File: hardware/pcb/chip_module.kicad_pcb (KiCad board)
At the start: 6 copper layers, 150 x 140 mm, 201 parts, among them J12 BTB_DAUGHTER

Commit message: latest boards 2 pcb first route
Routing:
- net +5V_A: track 8.44 -> 328.6 mm, vias 0 -> 17
- net DET_REF: track 1.00 -> 303.8 mm, vias 1 -> 3
- net DET_IN56: track 1.00 -> 261.4 mm, vias 1 -> 7
- net DET_IN61: track 1.00 -> 252.0 mm, vias 1 -> 6
- net DET_IN25: track 1.00 -> 239.3 mm, vias 1 -> 10
- net DET_IN30: track 1.00 -> 237.6 mm, vias 1 -> 6
- net DET_IN31: track 1.00 -> 235.3 mm, vias 1 -> 5
- net DET_IN16: track 1.00 -> 234.6 mm, vias 1 -> 10
- net DET_IN48: track 1.00 -> 230.7 mm, vias 1 -> 9
- net DET_IN20: track 1.00 -> 227.8 mm, vias 1 -> 5
- net DET_IN55: track 1.00 -> 227.3 mm, vias 1 -> 8
- net DET_IN23: track 1.00 -> 222.7 mm, vias 1 -> 8
- net DET_IN19: track 1.00 -> 221.4 mm, vias 1 -> 5
- net DET_IN17: track 1.00 -> 221.3 mm, vias 1 -> 9
- net DET_IN8: track 1.00 -> 203.2 mm, vias 1 -> 5
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
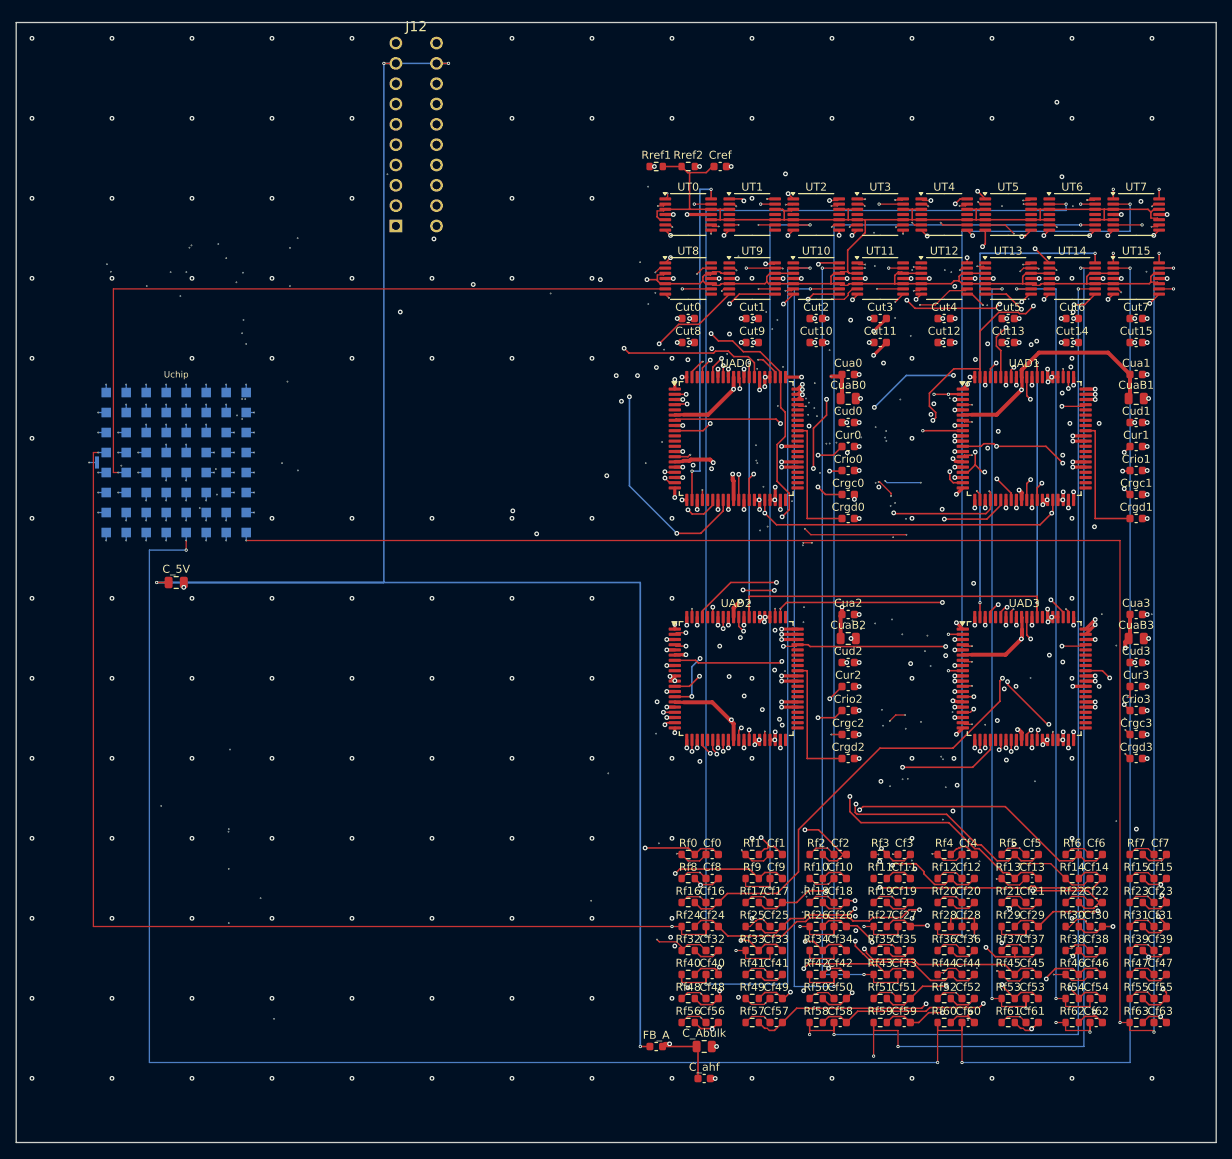
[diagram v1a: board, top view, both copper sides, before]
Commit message: pcb: head board DRC-clean for production (749 -> 0 violations)
- Remove 935 FreeRouting signal tracks incorrectly placed on In1.Cu (GND plane)
- Remove 41 sub-min-width FreeRouting stubs (0.1124mm < 0.15mm min) on F.Cu DET_IN*
- Remove redundant DET_IN30 through-via at (34.246,28.153): net stays fully
  connected via its In3 route + via at (132.083,22.955); clears 3 In3 clearance
  conflicts in the packed x~34 channel (DET_IN8/DET_IN19/DET_IN30)
- Remove zero-length FreeRouting stubs (<0.05mm)
- Relax hole-to-hole min 0.2495mm -> 0.22mm: HDI-appropriate for 0.10mm laser
  drills (JLCPCB/PCBWay HDI support 0.15mm); clears 3 hole_near_hole pairs
- Re-fill both copper zones (GND/In1, +3V3/In2) to clear stale-pour violations

Final: kicad-cli DRC 0 violations / 0 unconnected.
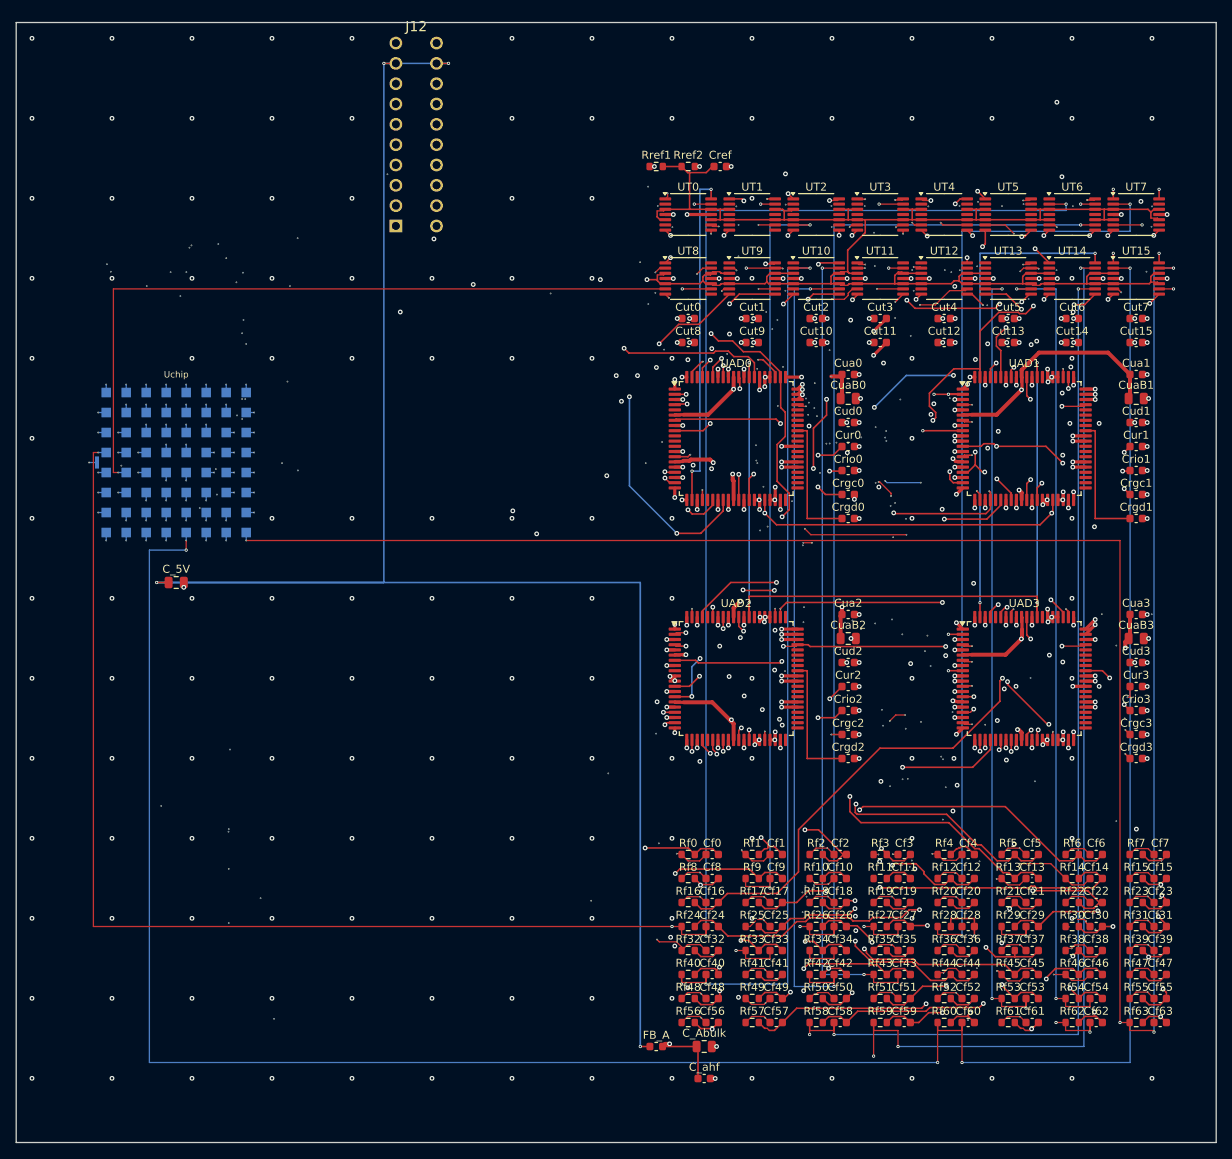
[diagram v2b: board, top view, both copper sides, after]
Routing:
- net DET_IN56: track 261.4 -> 100.7 mm
- net DET_TIA15: track 197.9 -> 38.2 mm
- net DET_TIA8: track 172.1 -> 17.7 mm
- net DET_IN0: track 175.3 -> 21.4 mm, vias 5 -> 3
- net DET_IN55: track 227.3 -> 102.0 mm
- net DET_IN35: track 194.0 -> 78.4 mm
- net DET_IN48: track 230.7 -> 118.4 mm
- net DET_IN16: track 234.6 -> 124.2 mm
- net DET_IN32: track 187.2 -> 77.8 mm
- net adc_miso: track 171.8 -> 66.7 mm
- net +5V_A: track 328.6 -> 226.7 mm
- net DET_IN30: track 237.6 -> 135.9 mm, vias 6 -> 5
- net DET_TIA7: track 142.5 -> 50.5 mm
- net DET_TIA31: track 162.4 -> 71.1 mm
- net DET_TIA33: track 97.5 -> 11.5 mm
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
